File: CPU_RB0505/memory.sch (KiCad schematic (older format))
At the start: 7 parts

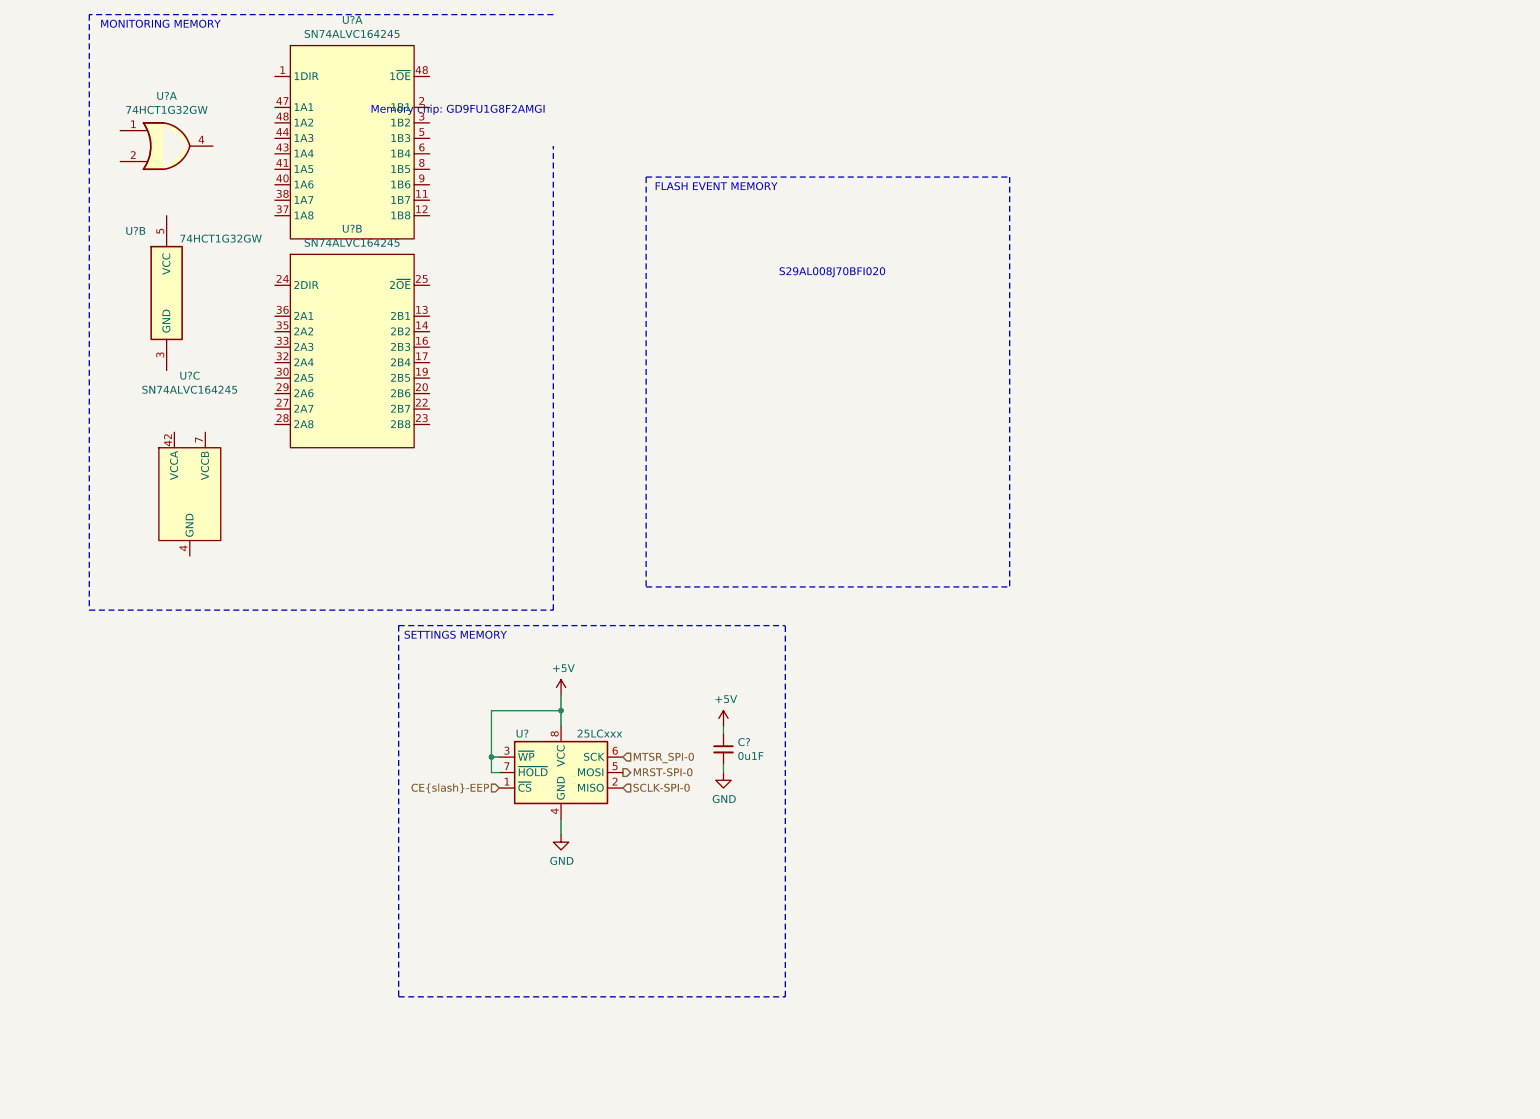
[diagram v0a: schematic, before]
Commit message: Update Memory page of CPU
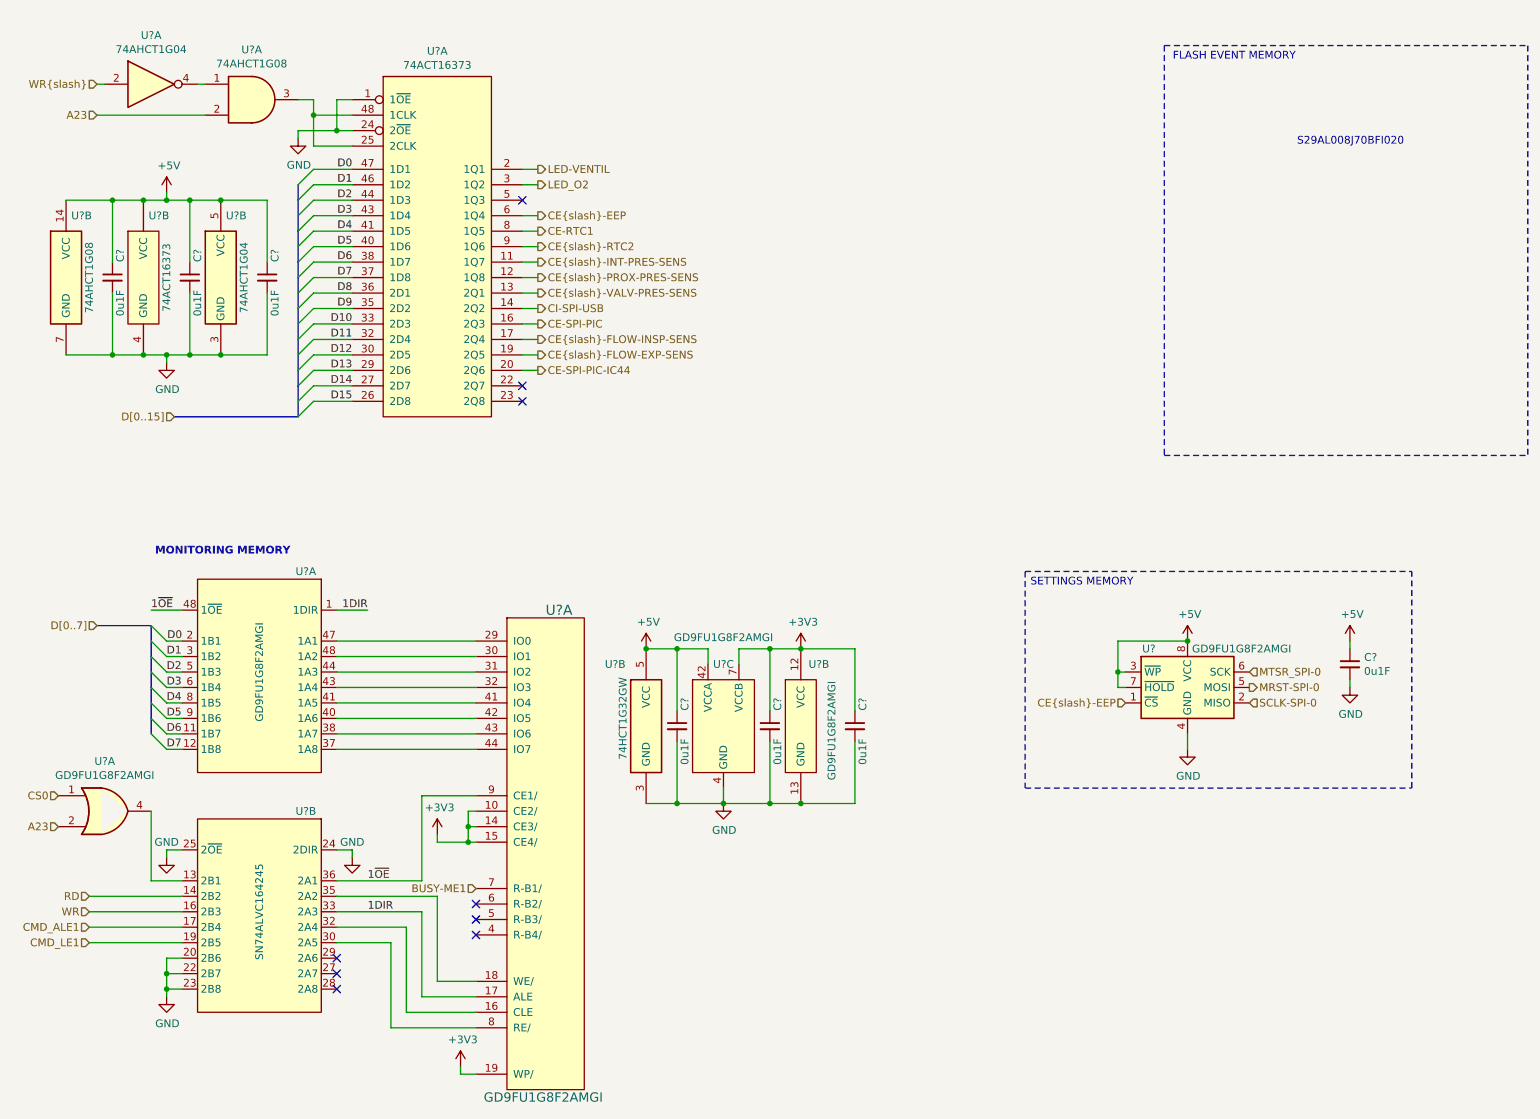
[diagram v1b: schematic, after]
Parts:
- added C? (x6): 0u1F, symbol Device:C_Small
- added U? (x2): GD9FU1G8F2AMGI, Package_SO:TSOP-I-48_18.4x12mm_P0.5mm, symbol CPU_RB0505:GD9FU1G8F2AMGI
- added U? (x2): 74ACT16373, symbol CPU_RB0505:74ACT16373
- added U? (x2): 74AHCT1G04, Package_TO_SOT_SMD:SOT-353_SC-70-5, symbol CPU_RB0505:74AHCT1G04
- added U? (x2): 74AHCT1G08, Package_TO_SOT_SMD:SOT-23-5, symbol CPU_RB0505:74AHCT1G08
- U?: value 25LCxxx -> GD9FU1G8F2AMGI; footprint (none) -> Package_SO:TSOP-I-48_18.4x12mm_P0.5mm
- U?: value 74HCT1G32GW -> GD9FU1G8F2AMGI; footprint (none) -> Package_SO:TSOP-I-48_18.4x12mm_P0.5mm
- U? (x2): value SN74ALVC164245 -> GD9FU1G8F2AMGI; footprint Package_SO:TSSOP-48_6.1x12.5mm_P0.5mm -> Package_SO:TSOP-I-48_18.4x12mm_P0.5mm
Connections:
- net +5V: now also U?.31 (VCCA), U?.42 (VCCA), U?.5 (VCC), C?.1, C?.1, C?.1, C?.1, U?.14 (VCC), U?.18 (VCC), U?.31 (VCC), U?.42 (VCC), U?.5 (VCC), U?.7 (VCC)
- net CE/-EEP: now also U?.6 (1Q4)
- net GND: now also U?.10 (GND), U?.15 (GND), U?.20 (2B6), U?.21 (GND), U?.22 (2B7), U?.23 (2B8), U?.24 (2DIR), U?.25 (2~OE), U?.28 (GND), U?.3 (GND), U?.34 (GND), U?.39 (GND), U?.4 (GND), U?.45 (GND), C?.2, C?.2, C?.2, C?.2, C?.2, C?.2, U?.1 (1~OE), U?.10 (GND), U?.13 (GND), U?.15 (GND), U?.21 (GND), U?.24 (2~OE), U?.28 (GND), U?.3 (GND), U?.34 (GND), U?.36 (GND), U?.39 (GND), U?.4 (GND), U?.45 (GND), U?.7 (GND)
- net CS0: now reaches U?.1
- net A23: now reaches U?.2
- net A23: now also U?.2
- net at U?.4: now also U?.13 (2B1)
- net 1DIR: now reaches U?.1 (1DIR)
- net 1DIR: now also U?.33 (2A3), U?.17 (ALE)
- net D6: now reaches U?.11 (1B7)
- net D6: now also U?.38 (1D7)
- net D7: now reaches U?.12 (1B8)
- net D7: now also U?.37 (1D8)
- net D0: now reaches U?.2 (1B1)
- net D0: now also U?.47 (1D1)
- net D1: now reaches U?.3 (1B2)
- net D1: now also U?.46 (1D2)
- net at U?.37 (1A8): now also U?.44 (IO7)
- net at U?.38 (1A7): now also U?.43 (IO6)
- net at U?.40 (1A6): now also U?.42 (IO5)
- net at U?.41 (1A5): now also U?.41 (IO4)
- net at U?.43 (1A4): now also U?.32 (IO3)
- net at U?.44 (1A3): now also U?.31 (IO2)
- net at U?.47 (1A1): now also U?.29 (IO0)
- net 1~OE: now reaches U?.48 (1~OE)
- net 1~OE: now also U?.36 (2A1), U?.9 (CE1/)
- net D2: now reaches U?.5 (1B3)
- net D2: now also U?.44 (1D3)
- net D3: now reaches U?.6 (1B4)
- net D3: now also U?.43 (1D4)
- net D4: now reaches U?.8 (1B5)
- net D4: now also U?.41 (1D5)
- net D5: now reaches U?.9 (1B6)
- net D5: now also U?.40 (1D6)
- net RD: now reaches U?.14 (2B2)
- net WR: now reaches U?.16 (2B3)
- net CMD_ALE1: now reaches U?.17 (2B4)
- net CMD_LE1: now reaches U?.19 (2B5)
- net at U?.30 (2A5): now also U?.8 (RE/)
- net at U?.32 (2A4): now also U?.16 (CLE)
- net at U?.35 (2A2): now also U?.18 (WE/)
- net +3V3: now reaches U?.16 (VCCB), U?.7 (VCCB)
- net +3V3: now also C?.1, C?.1, U?.10 (CE2/), U?.12 (VCC), U?.14 (CE3/), U?.15 (CE4/), U?.19 (WP/), U?.37 (VCC)
- new net: U?.1 (NC1), U?.11 (NC4), U?.2 (NC2), U?.20 (NC5), U?.21 (NC6), U?.22 (NC7), U?.23 (NC8), U?.24 (NC9), U?.25 (NC10), U?.26 (NC11), U?.27 (NC12), U?.28 (NC13), U?.3 (NC3), U?.33 (NC14), U?.34 (NC15), U?.35 (NC16), U?.38 (NC17), U?.39 (NC18), U?.40 (NC19), U?.45 (NC20), U?.46 (NC21), U?.47 (NC22), U?.48 (NC23)
- new net: U?.30 (IO1), U?.48 (1~OE)
- new net: U?.25 (2CLK), U?.3, U?.48 (1CLK)
- new net: U?.1, U?.4
- new net BUSY-ME1: U?.7 (R-B1/)
- new net CE-RTC1: U?.8 (1Q5)
- new net CE-SPI-PIC: U?.16 (2Q3)
- new net CE-SPI-PIC-IC44: U?.20 (2Q6)
- new net CE/-FLOW-EXP-SENS: U?.19 (2Q5)
- new net CE/-FLOW-INSP-SENS: U?.17 (2Q4)
- new net CE/-INT-PRES-SENS: U?.11 (1Q7)
- new net CE/-PROX-PRES-SENS: U?.12 (1Q8)
- new net CE/-RTC2: U?.9 (1Q6)
- new net CE/-VALV-PRES-SENS: U?.13 (2Q1)
- new net CI-SPI-USB: U?.14 (2Q2)
- new net D10: U?.33 (2D3)
- new net D11: U?.32 (2D4)
- new net D12: U?.30 (2D5)
- new net D13: U?.29 (2D6)
- new net D14: U?.27 (2D7)
- new net D15: U?.26 (2D8)
- new net D8: U?.36 (2D1)
- new net D9: U?.35 (2D2)
- new net LED-VENTIL: U?.2 (1Q1)
- new net LED_O2: U?.3 (1Q2)
- new net WR/: U?.2
- no-connect marks 0 -> 9
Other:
- note removed: "Memory chip: GD9FU1G8F2AMGI"
- moved on the sheet: C?, U?, U?A, U?B, U?C
